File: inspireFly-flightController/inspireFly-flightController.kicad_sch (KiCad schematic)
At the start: 21 parts, among them SW1 SW_Push, SW2 SW_Push, U1 STM32U595VITx, Y1 ABS07-32.768KHZ-T

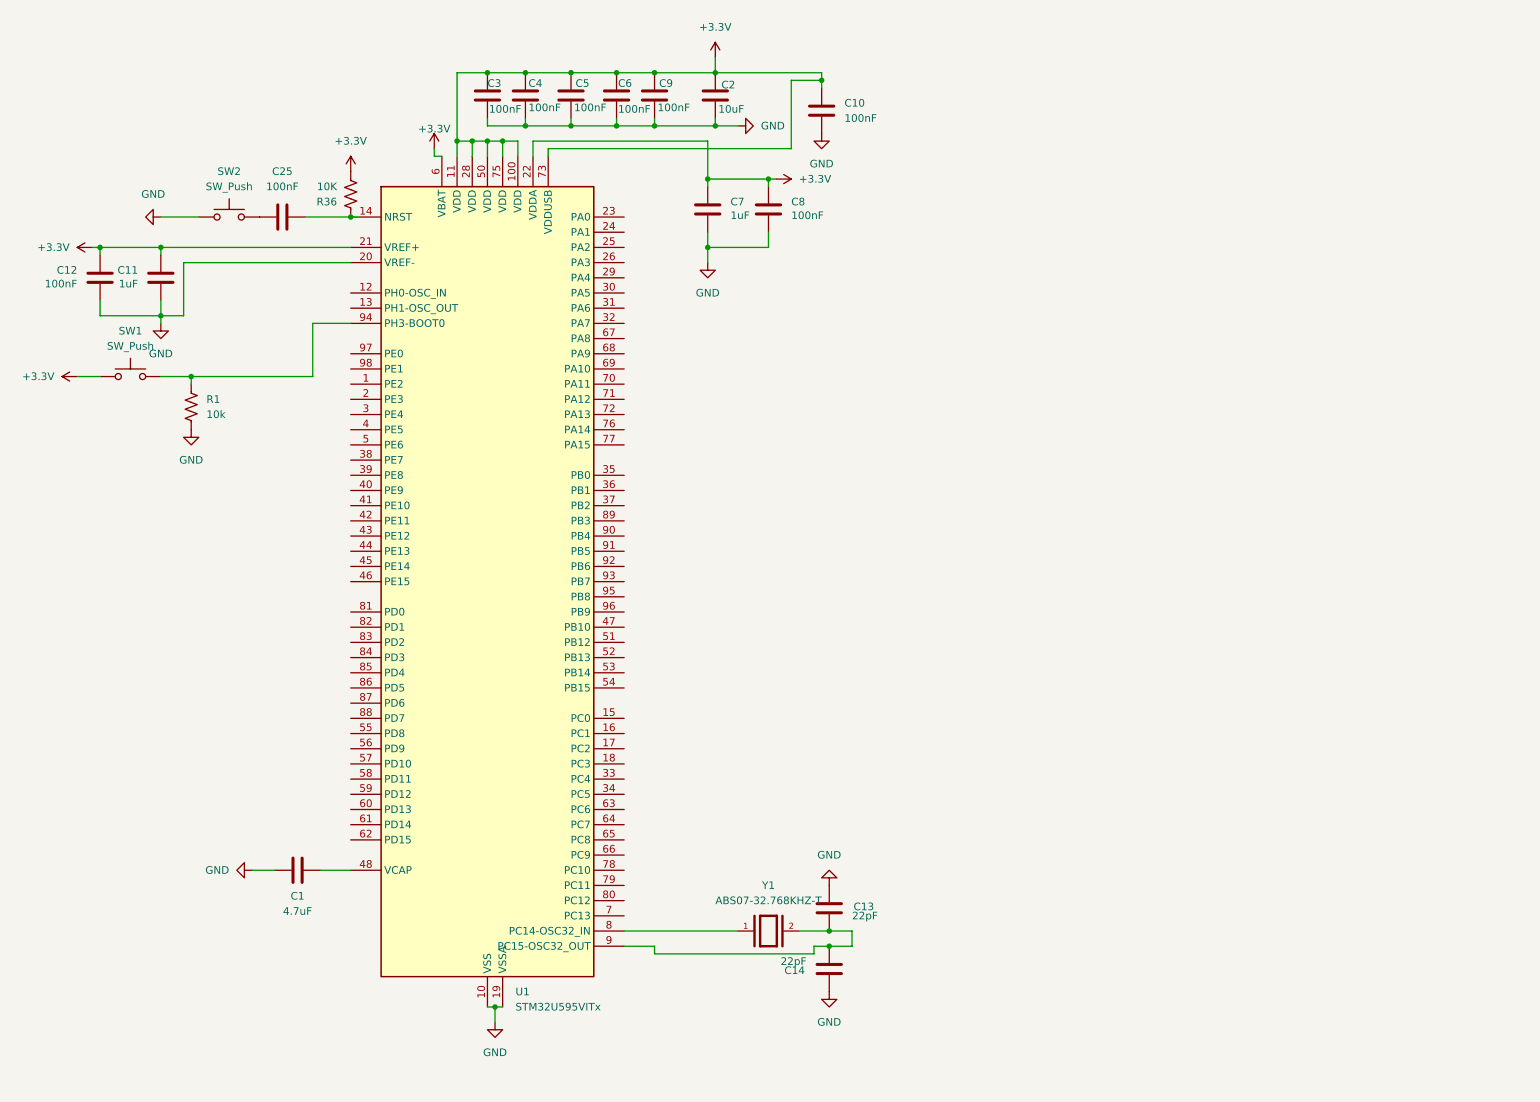
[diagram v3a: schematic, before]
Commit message: added st-link connector
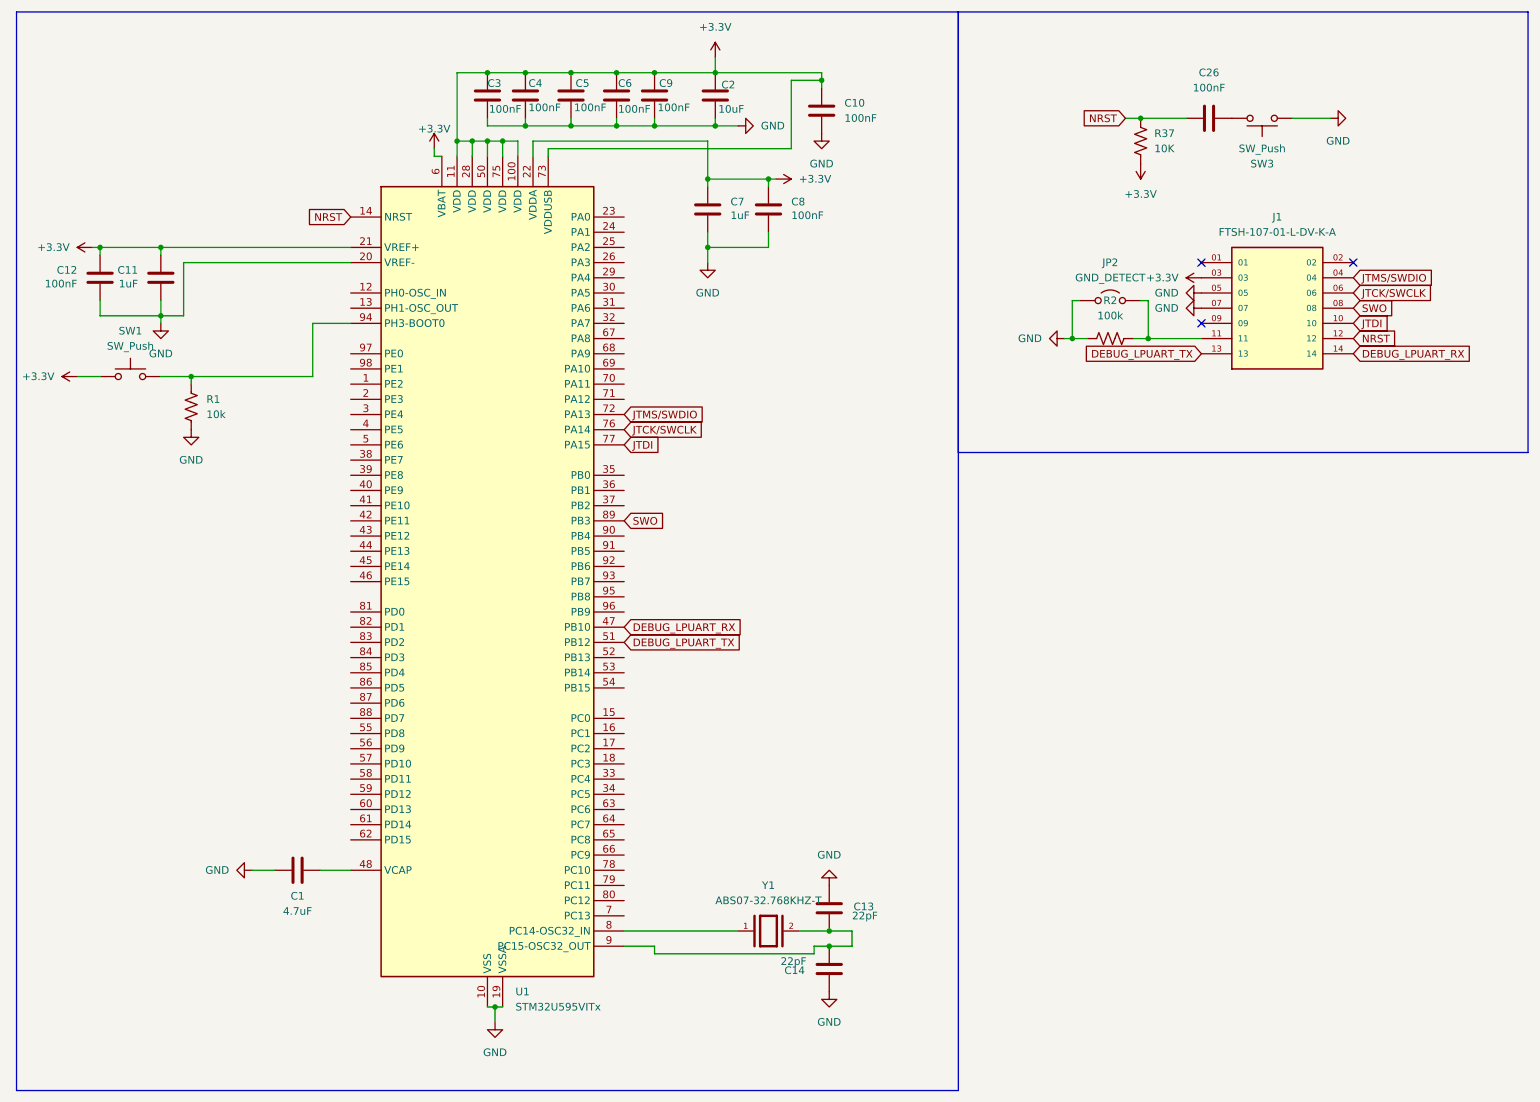
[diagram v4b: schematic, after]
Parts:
- removed C25: 100nF, Capacitor_SMD:C_0402_1005Metric_Pad0.74x0.62mm_HandSolder, symbol Device:C
- removed R36: 10K, Resistor_SMD:R_0402_1005Metric_Pad0.72x0.64mm_HandSolder, symbol Device:R_US
- removed SW2: SW_Push, inspireFly-EPS-footprints:SW_PTS810_SJM_250_SMTR_LFS, symbol Switch:SW_Push
- added C26: 100nF, Capacitor_SMD:C_0402_1005Metric_Pad0.74x0.62mm_HandSolder, symbol Device:C
- added J1: FTSH-107-01-L-DV-K-A, FTSH-107-01-L-DV-K-A:SAMTEC_FTSH-107-01-L-DV-K-A, symbol flightController:FTSH-107-01-L-DV-K-A
- added JP2: GND_DETECT, inspirefly:SmallJumper, symbol Jumper:Jumper_2_Open
- added R2: 100k, symbol Device:R_US
- added R37: 10K, Resistor_SMD:R_0402_1005Metric_Pad0.72x0.64mm_HandSolder, symbol Device:R_US
- added SW3: SW_Push, inspireFly-EPS-footprints:SW_PTS810_SJM_250_SMTR_LFS, symbol Switch:SW_Push
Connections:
- net +3.3V: now also J1.03, R37.2
- net GND: now also J1.05, J1.07, JP2.1 (A), R2.1, SW3.1
- net NRST: now reaches U1.14 (NRST)
- net NRST: now also C26.2, J1.12, R37.1
- net DEBUG_LPUART_RX: now reaches U1.47 (PB10)
- net DEBUG_LPUART_RX: now also J1.14
- net DEBUG_LPUART_TX: now reaches U1.51 (PB12)
- net DEBUG_LPUART_TX: now also J1.13
- net JTMS/SWDIO: now reaches U1.72 (PA13)
- net JTMS/SWDIO: now also J1.04
- net JTCK/SWCLK: now reaches U1.76 (PA14)
- net JTCK/SWCLK: now also J1.06
- net JTDI: now reaches U1.77 (PA15)
- net JTDI: now also J1.10
- net SWO: now reaches U1.89 (PB3)
- net SWO: now also J1.08
- new net: C26.1, SW3.2
- new net: J1.11, JP2.2 (B), R2.2
- no-connect marks 0 -> 3

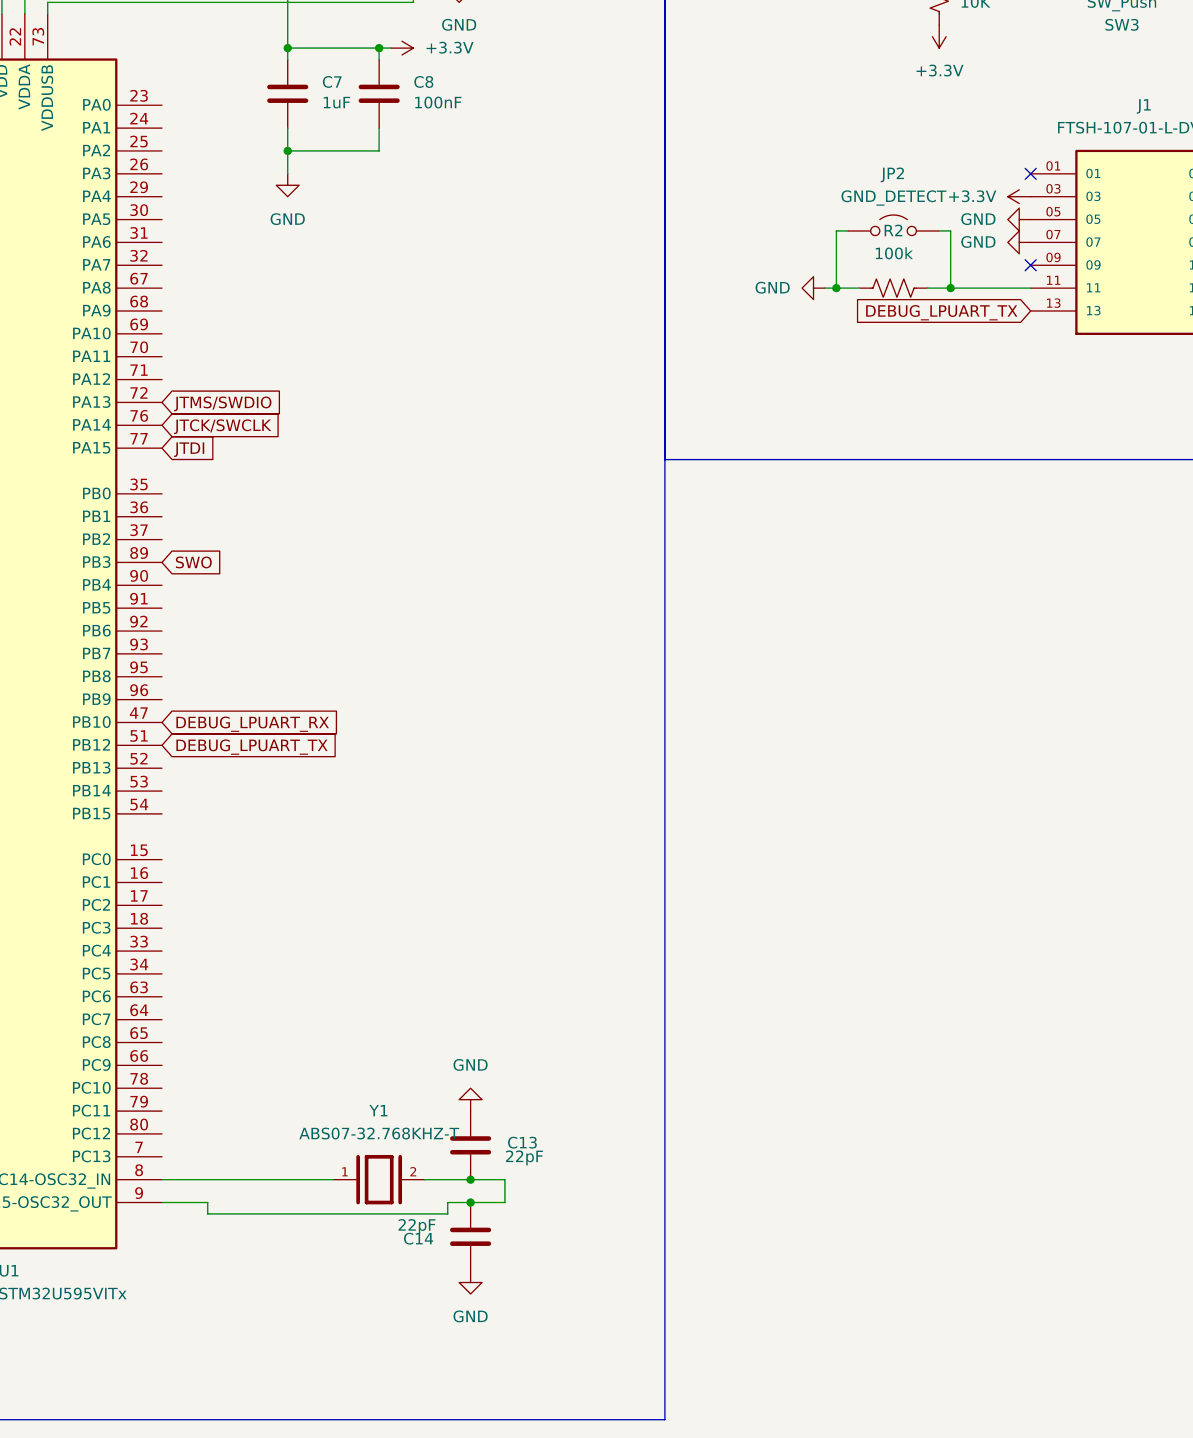
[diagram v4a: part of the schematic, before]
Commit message: added board edges
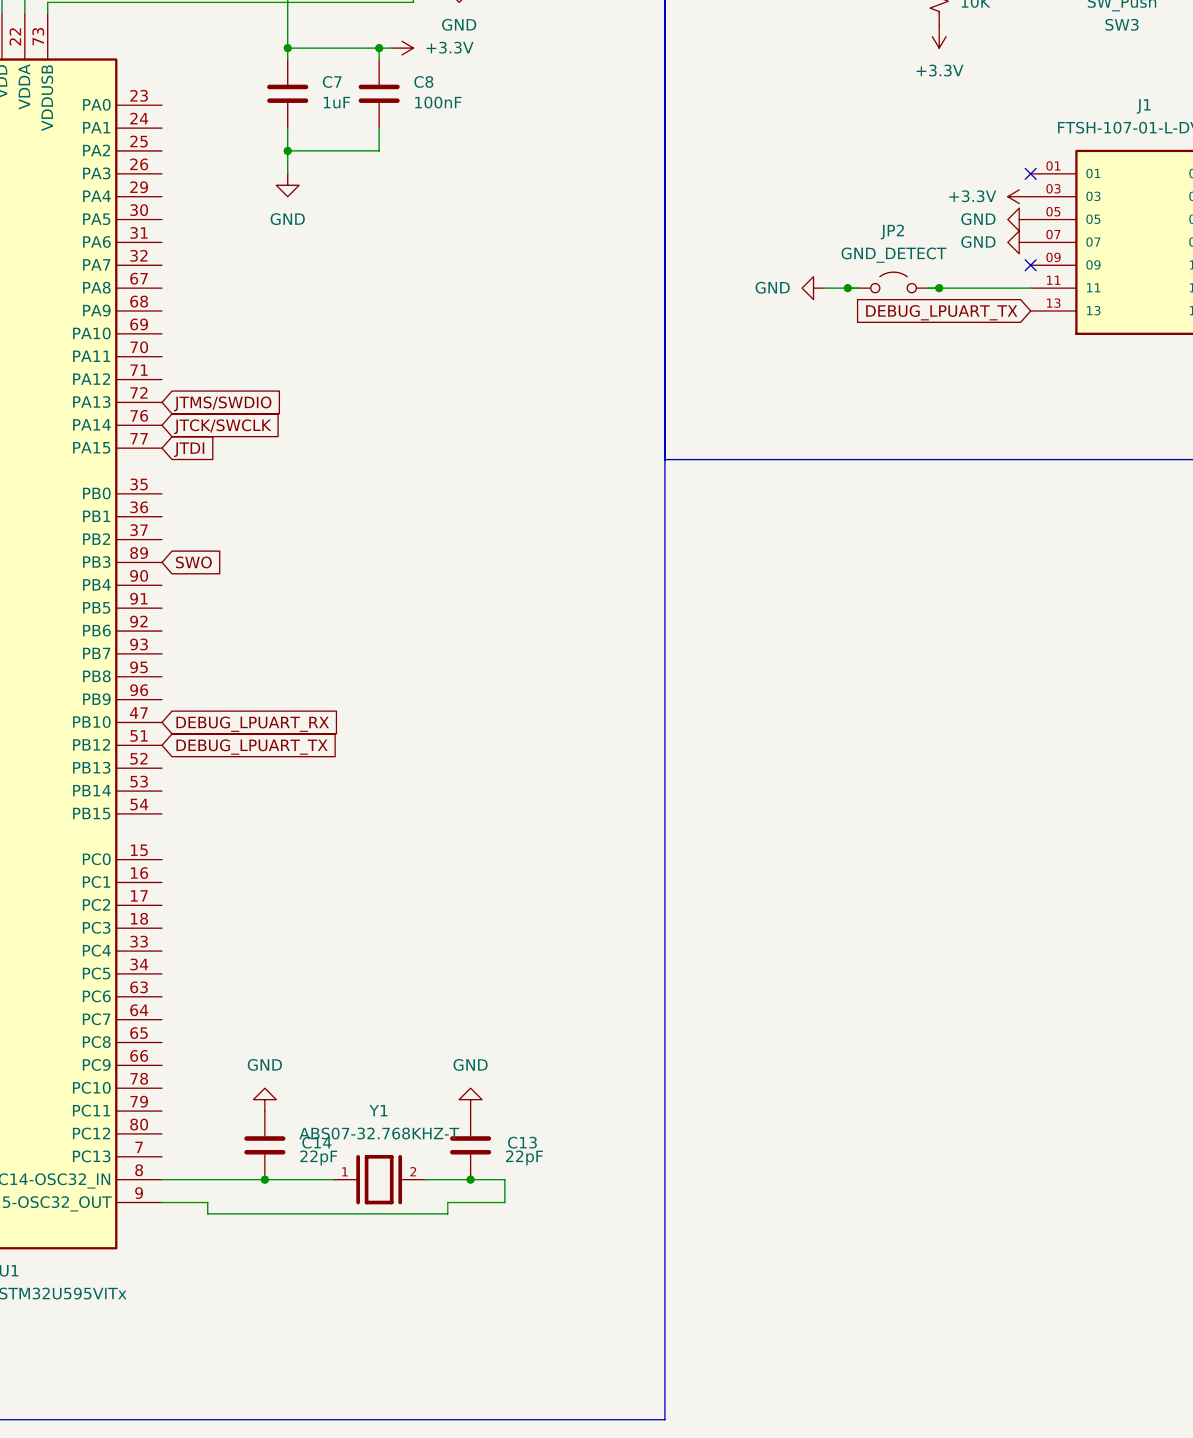
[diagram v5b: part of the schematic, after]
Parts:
- removed R2: 100k, symbol Device:R_US
- C1, C10, C13, C14, C2: footprint (none) -> Capacitor_SMD:C_0402_1005Metric_Pad0.74x0.62mm_HandSolder
- J1: footprint FTSH-107-01-L-DV-K-A:SAMTEC_FTSH-107-01-L-DV-K-A -> inspirefly:SAMTEC_FTSH-107-01-L-DV-K-A
- R1: footprint (none) -> Resistor_SMD:R_0402_1005Metric_Pad0.72x0.64mm_HandSolder
- SW1: footprint (none) -> inspireFly-EPS-footprints:SW_PTS810_SJM_250_SMTR_LFS
- Y1: footprint ABS07-32.768KHZ-T:XTAL_ABS07-32.768KHZ-T -> inspirefly:XTAL_ABS07-32.768KHZ-T
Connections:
- net at C13.2, U1.9 (PC15-OSC32_OUT), Y1.2: no longer C14.2
- net at U1.8 (PC14-OSC32_IN), Y1.1: now also C14.2
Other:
- moved on the sheet: C14, JP2
